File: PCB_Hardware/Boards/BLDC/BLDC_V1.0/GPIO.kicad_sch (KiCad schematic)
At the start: 16 parts, among them J8 Conn_02x06_Odd_Even, J9 Conn_01x06_Socket, Q12 BSS84, U14 SRV05-4, U15 TS5A3159ADBVR, U8 SRV05-4, U9 SRV05-4

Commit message: Add DBcan transport refactor, BLDC V1.0 schematic + sim work, HAL submodule
- DBcan: replace bare-register driver with vendor-agnostic transport abstraction (core/, transports/, refactored bootloader driver, README)
- Add stm32g4xx_hal_driver as Firmware/libs submodule
- Add HAL config for BLDC board (stm32g4xx_hal_conf.h)
- BLDC V1.0: schematic edits across 10 sheets (footprint assignments, repositioning); design-doc README (gate-driver constraints, FET selection / TPH3R70APL, thermal analysis)
- ngspice simulation workflow (cap sweeps, half-bridge slow turn-on)
- Ignore .obsidian/ vault state and large simulation CSV exports
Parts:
- F1, F2, F4, F5: footprint (none) -> Fuse:Fuse_0805_2012Metric
- R25, R26: footprint (none) -> Resistor_SMD:R_0402_1005Metric
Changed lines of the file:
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@@
 			)
 		)
-		(property "Footprint" ""
+		(property "Footprint" "Resistor_SMD:R_0402_1005Metric"
 			(at 66.802 49.53 90)
 			(hide yes)
@@
 			)
 		)
-		(property "Footprint" ""
+		(property "Footprint" "Fuse:Fuse_0805_2012Metric"
 			(at 173.99 35.56 0)
 			(hide yes)
@@
 			)
 		)
-		(property "Footprint" ""
+		(property "Footprint" "Fuse:Fuse_0805_2012Metric"
 			(at 163.83 113.03 0)
 			(hide yes)
@@
 			)
 		)
-		(property "Footprint" ""
+		(property "Footprint" "Resistor_SMD:R_0402_1005Metric"
 			(at 87.122 49.53 90)
 			(hide yes)
@@
 			)
 		)
-		(property "Footprint" ""
+		(property "Footprint" "Fuse:Fuse_0805_2012Metric"
 			(at 134.62 44.45 0)
 			(hide yes)
@@
 			)
 		)
-		(property "Footprint" ""
+		(property "Footprint" "Fuse:Fuse_0805_2012Metric"
 			(at 184.15 113.03 0)
 			(hide yes)

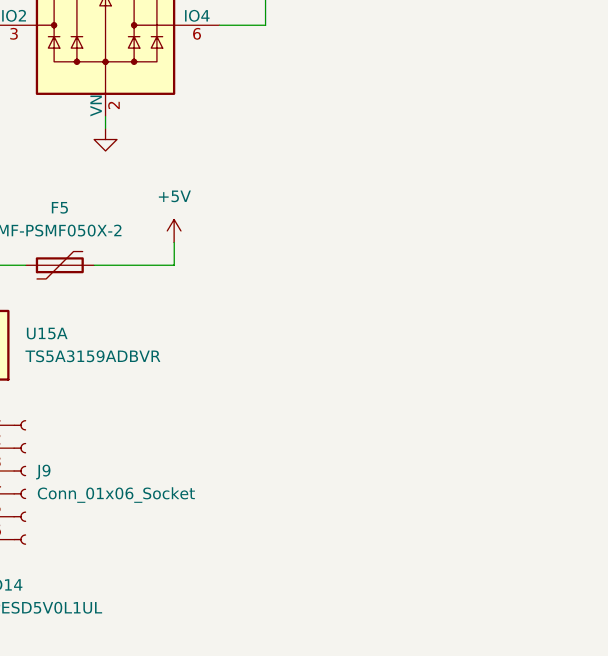
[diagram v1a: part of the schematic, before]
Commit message: Created organization around the symbol lib and did a first pass layout of the BDLC
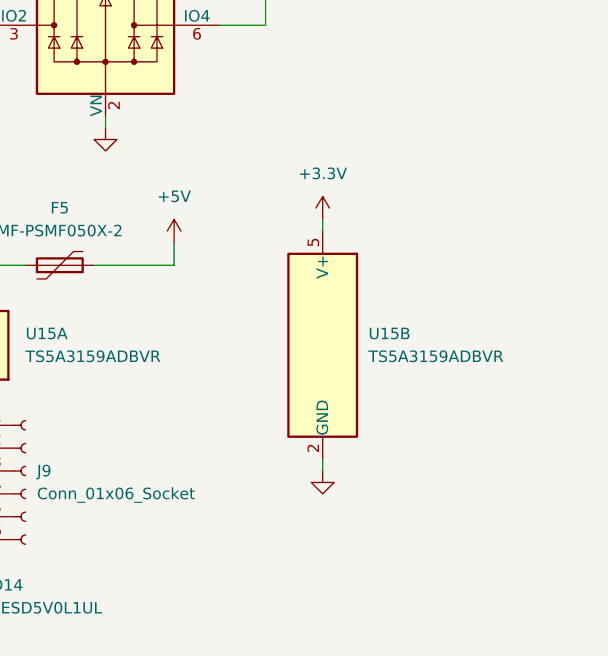
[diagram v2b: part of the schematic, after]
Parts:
- added unit 2 of U15
- J8: footprint (none) -> Connector_JST:JST_PUD_S12B-PUDSS-1_2x06_P2.00mm_Horizontal
- J9: footprint (none) -> Connector_JST:JST_GH_SM06B-GHS-TB_1x06-1MP_P1.25mm_Horizontal
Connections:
- net +3.3V: now also U15.5 (V+)
- net GND: now also U15.2 (GND)

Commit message: complete redo of the BLDC layout
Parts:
- J8: footprint Connector_JST:JST_PUD_S12B-PUDSS-1_2x06_P2.00mm_Horizontal -> Connector_JST:JST_PUD_B12B-PUDSS_2x06_P2.00mm_Vertical
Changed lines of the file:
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@@
 			)
 		)
-		(property "Footprint" "Connector_JST:JST_PUD_S12B-PUDSS-1_2x06_P2.00mm_Horizontal"
+		(property "Footprint" "Connector_JST:JST_PUD_B12B-PUDSS_2x06_P2.00mm_Vertical"
 			(at 157.48 53.34 0)
 			(hide yes)
